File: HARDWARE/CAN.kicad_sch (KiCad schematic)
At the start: 5 parts, among them U6 MCP2562-H-SN

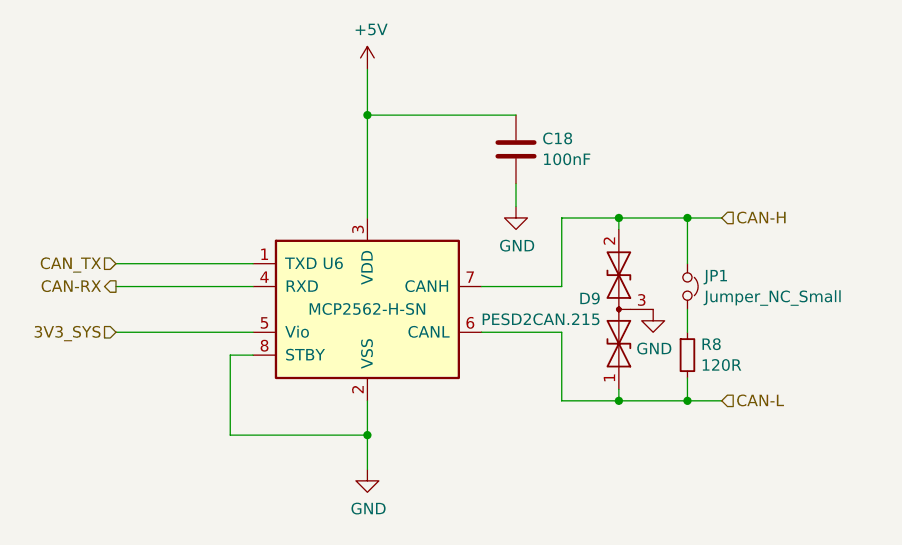
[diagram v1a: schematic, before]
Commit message: Align components on the PCB
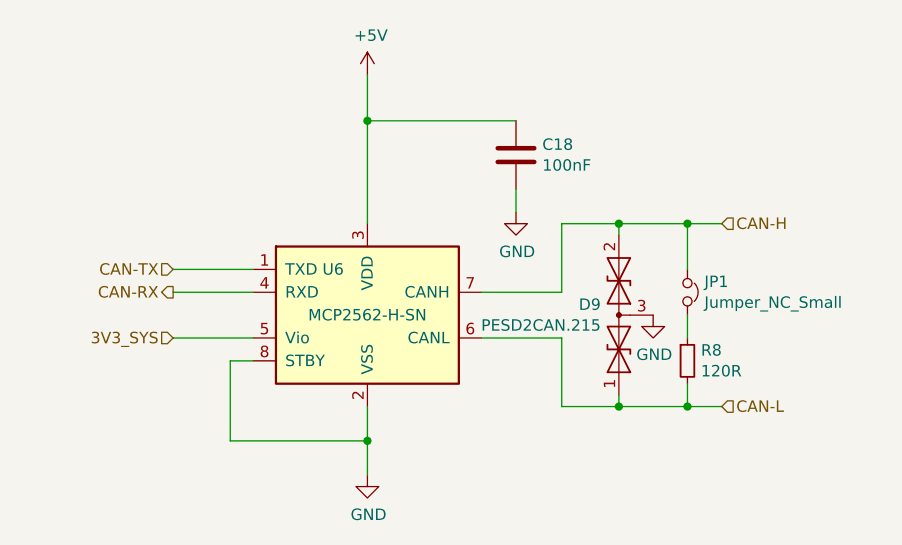
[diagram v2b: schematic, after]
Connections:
- net CAN_TX renamed CAN-TX
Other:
- company: (none) -> PUT Motorsport
- moved on the sheet: C18, D9, JP1, R8, U6

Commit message: KiCad project refactor
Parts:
- D9: symbol Device:D_TVS_x2_AAC -> D_TVS_x2_AAC:D_TVS_x2_AAC-Device
- JP1: symbol Device:Jumper_NC_Small -> Jumper_NC_Small:Jumper_NC_Small
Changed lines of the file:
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@@
     )
   )
-  (symbol (lib_id "Device:D_TVS_x2_AAC") (at 158.75 85.09 90) (unit 1)
+  (symbol (lib_id "D_TVS_x2_AAC:D_TVS_x2_AAC-Device") (at 158.75 85.09 90) (unit 1)
     (in_bom yes) (on_board yes) (dnp no)
     (property "Reference" "D9" (at 156.7434 83.9216 90)
@@
     )
   )
-  (symbol (lib_id "Device:Jumper_NC_Small") (at 166.37 82.55 270) (unit 1)
+  (symbol (lib_id "Jumper_NC_Small:Jumper_NC_Small") (at 166.37 82.55 270) (unit 1)
     (in_bom yes) (on_board yes) (dnp no)
     (property "Reference" "JP1" (at 168.2496 81.3816 90)

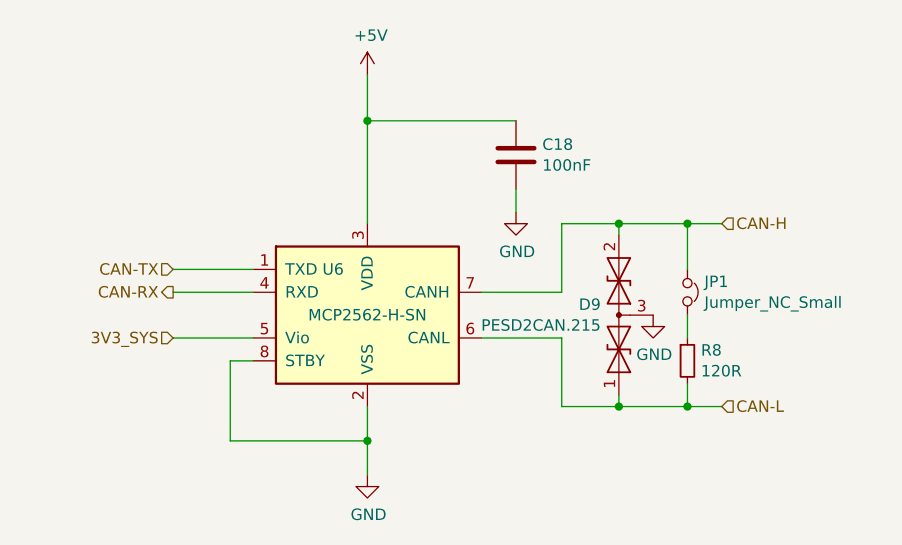
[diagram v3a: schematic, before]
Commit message: Route PCB tracks
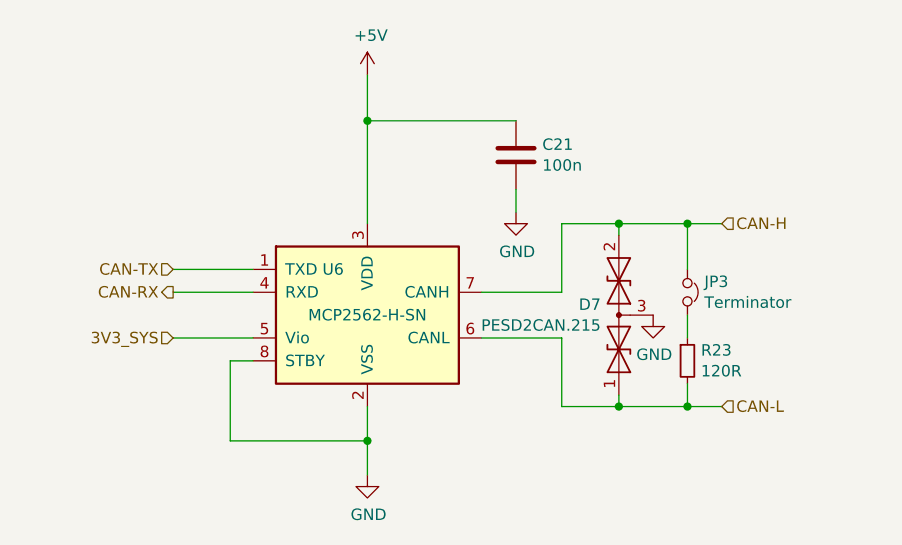
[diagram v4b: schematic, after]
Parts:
- C21: renamed from C18; value 100nF -> 100n
- JP3: renamed from JP1; value Jumper_NC_Small -> Terminator
- renumbered D9 to D7, R8 to R23
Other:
- company: PUT Motorsport -> S. Sambor
- title: (none) -> CAN Communication
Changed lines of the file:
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@@
   (paper "A4")
   (title_block
-    (company "PUT Motorsport")
-    (comment 1 "Patryk Gawron")
+    (title "CAN Communication")
+    (date "2023-04-22")
+    (rev "2.0")
+    (company "S. Sambor")
+    (comment 1 "J. Jurczak")
+    (comment 2 "P. Gawron")
+    (comment 3 "I. Kajdan")
   )
   (junction (at 130.81 99.06) (diameter 0) (color 0 0 0 0)
@@
   (symbol (lib_id "power:GND") (at 147.32 73.66 0) (unit 1)
     (in_bom yes) (on_board yes) (dnp no)
-    (property "Reference" "#PWR020" (at 147.32 80.01 0)
+    (property "Reference" "#PWR032" (at 147.32 80.01 0)
       (effects (font (size 1.27 1.27)) hide)
     )
@@
       (project "APPS"
         (path "/fc4ad874-c922-4070-89f9-7262080469d8/00000000-0000-0000-0000-00005f60f83f"
-          (reference "#PWR020") (unit 1)
+          (reference "#PWR032") (unit 1)
         )
       )
@@
   (symbol (lib_id "power:GND") (at 130.81 102.87 0) (unit 1)
     (in_bom yes) (on_board yes) (dnp no)
-    (property "Reference" "#PWR022" (at 130.81 109.22 0)
+    (property "Reference" "#PWR031" (at 130.81 109.22 0)
       (effects (font (size 1.27 1.27)) hide)
     )
@@
       (project "APPS"
         (path "/fc4ad874-c922-4070-89f9-7262080469d8/00000000-0000-0000-0000-00005f60f83f"
-          (reference "#PWR022") (unit 1)
+          (reference "#PWR031") (unit 1)
         )
       )
@@
   (symbol (lib_id "power:+5V") (at 130.81 58.42 0) (unit 1)
     (in_bom yes) (on_board yes) (dnp no)
-    (property "Reference" "#PWR019" (at 130.81 62.23 0)
+    (property "Reference" "#PWR030" (at 130.81 62.23 0)
       (effects (font (size 1.27 1.27)) hide)
     )
@@
       (project "APPS"
         (path "/fc4ad874-c922-4070-89f9-7262080469d8/00000000-0000-0000-0000-00005f60f83f"
-          (reference "#PWR019") (unit 1)
+          (reference "#PWR030") (unit 1)
         )
       )
@@
   (symbol (lib_id "Device:C") (at 147.32 67.31 0) (unit 1)
     (in_bom yes) (on_board yes) (dnp no)
-    (property "Reference" "C18" (at 150.241 66.1416 0)
-      (effects (font (size 1.27 1.27)) (justify left))
-    )
-    (property "Value" "100nF" (at 150.241 68.453 0)
+    (property "Reference" "C21" (at 150.241 66.1416 0)
+      (effects (font (size 1.27 1.27)) (justify left))
+    )
+    (property "Value" "100n" (at 150.241 68.453 0)
       (effects (font (size 1.27 1.27)) (justify left))
     )
@@
       (project "APPS"
         (path "/fc4ad874-c922-4070-89f9-7262080469d8/00000000-0000-0000-0000-00005f60f83f"
-          (reference "C18") (unit 1)
+          (reference "C21") (unit 1)
         )
       )
@@
   (symbol (lib_id "Device:R_Small") (at 166.37 90.17 0) (unit 1)
     (in_bom yes) (on_board yes) (dnp no)
-    (property "Reference" "R8" (at 167.8686 89.0016 0)
+    (property "Reference" "R23" (at 167.8686 89.0016 0)
       (effects (font (size 1.27 1.27)) (justify left))
     )
@@
       (project "APPS"
         (path "/fc4ad874-c922-4070-89f9-7262080469d8/00000000-0000-0000-0000-00005f60f83f"
-          (reference "R8") (unit 1)
+          (reference "R23") (unit 1)
         )
       )
@@
   (symbol (lib_id "D_TVS_x2_AAC:D_TVS_x2_AAC-Device") (at 158.75 85.09 90) (unit 1)
     (in_bom yes) (on_board yes) (dnp no)
-    (property "Reference" "D9" (at 156.7434 83.9216 90)
+    (property "Reference" "D7" (at 156.7434 83.9216 90)
       (effects (font (size 1.27 1.27)) (justify left))
     )
@@
       (project "APPS"
         (path "/fc4ad874-c922-4070-89f9-7262080469d8/00000000-0000-0000-0000-00005f60f83f"
-          (reference "D9") (unit 1)
+          (reference "D7") (unit 1)
         )
       )
@@
   (symbol (lib_id "power:GND") (at 162.56 85.09 0) (unit 1)
     (in_bom yes) (on_board yes) (dnp no)
-    (property "Reference" "#PWR021" (at 162.56 91.44 0)
+    (property "Reference" "#PWR033" (at 162.56 91.44 0)
       (effects (font (size 1.27 1.27)) hide)
     )
@@
       (project "APPS"
         (path "/fc4ad874-c922-4070-89f9-7262080469d8/00000000-0000-0000-0000-00005f60f83f"
-          (reference "#PWR021") (unit 1)
+          (reference "#PWR033") (unit 1)
         )
       )
@@
   (symbol (lib_id "Jumper_NC_Small:Jumper_NC_Small") (at 166.37 82.55 270) (unit 1)
     (in_bom yes) (on_board yes) (dnp no)
-    (property "Reference" "JP1" (at 168.2496 81.3816 90)
-      (effects (font (size 1.27 1.27)) (justify left))
-    )
-    (property "Value" "Jumper_NC_Small" (at 168.2496 83.693 90)
+    (property "Reference" "JP3" (at 168.2496 81.3816 90)
+      (effects (font (size 1.27 1.27)) (justify left))
+    )
+    (property "Value" "Terminator" (at 168.2496 83.693 90)
       (effects (font (size 1.27 1.27)) (justify left))
     )
@@
       (project "APPS"
         (path "/fc4ad874-c922-4070-89f9-7262080469d8/00000000-0000-0000-0000-00005f60f83f"
-          (reference "JP1") (unit 1)
-        )
-      )
+          (reference "JP3") (unit 1)
+        )
+      )
